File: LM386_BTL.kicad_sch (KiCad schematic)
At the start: 31 parts, among them J1 IN, J2 L_OUT, J3 R_OUT, J4 POWER, U1 LM386, U2 LM386, U3 LM386, U4 LM386

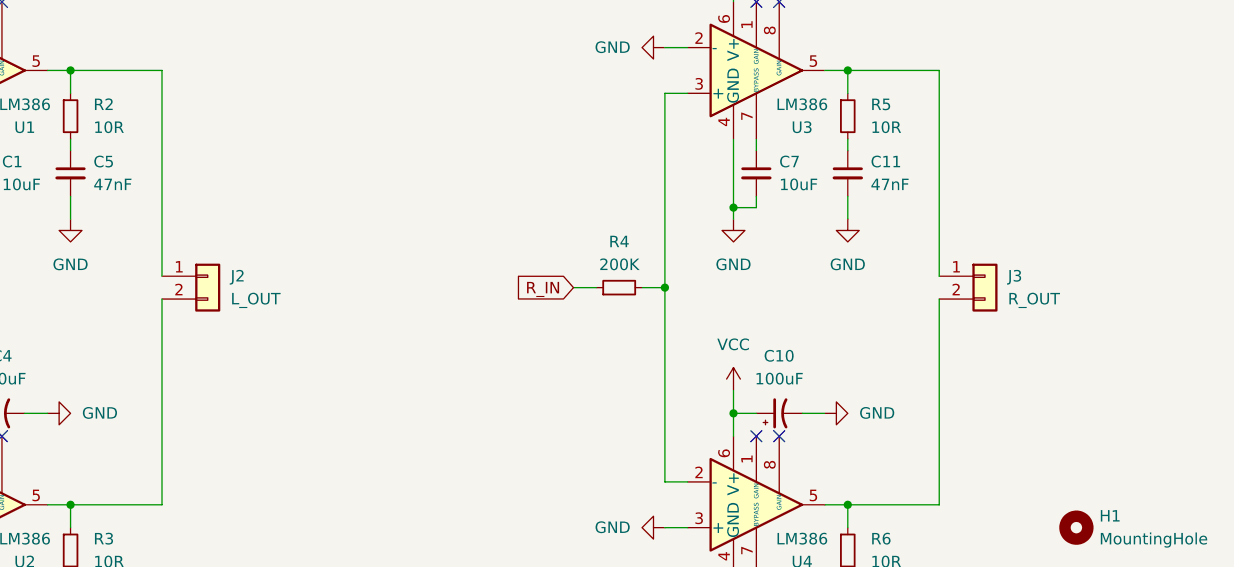
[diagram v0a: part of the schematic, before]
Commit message: Swap positive and negative amplifier position prevent from oscillation
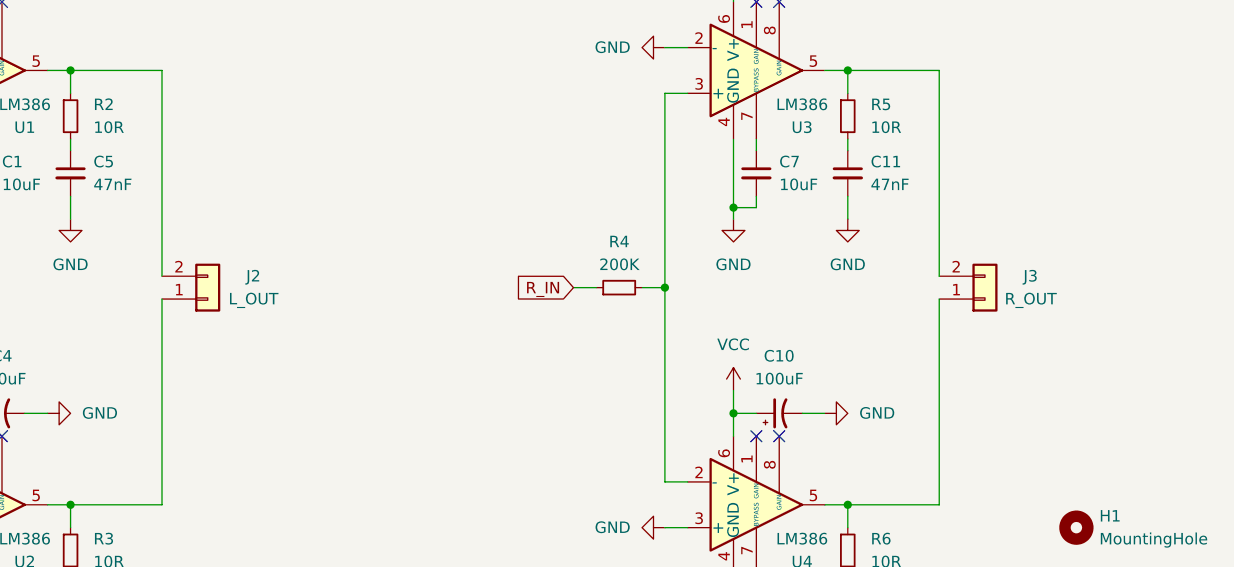
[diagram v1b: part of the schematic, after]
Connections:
- net at R5.1, U3.5: now also J3.2 (Pin_2); no longer J3.1 (Pin_1)
- net at R6.1, U4.5: now also J3.1 (Pin_1); no longer J3.2 (Pin_2)
- net at R2.1, U1.5: now also J2.2 (Pin_2); no longer J2.1 (Pin_1)
- net at R3.1, U2.5: now also J2.1 (Pin_1); no longer J2.2 (Pin_2)
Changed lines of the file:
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@@
   (title_block
     (title "The Ultimate LM386 BTL Amplifier")
-    (date "2022-12-18")
+    (date "2022-12-20")
     (rev "1.0")
     (company "DANCHOUZHOU")
@@
     (pin "1")
   )
-  (symbol (lib_id "Connector_Generic:Conn_01x02") (at 134.62 88.9 0) (unit 1)
-    (in_bom yes) (on_board yes) (fields_autoplaced)
-    (property "Reference" "J2" (id 0) (at 137.16 88.8999 0)
-      (effects (font (size 1.27 1.27)) (justify left))
-    )
-    (property "Value" "L_OUT" (id 1) (at 137.16 91.4399 0)
-      (effects (font (size 1.27 1.27)) (justify left))
-    )
-    (property "Footprint" "Connector_JST:JST_PH_B2B-PH-K_1x02_P2.00mm_Vertical" (id 2) (at 134.62 88.9 0)
-      (effects (font (size 1.27 1.27)) hide)
-    )
-    (property "Datasheet" "~" (id 3) (at 134.62 88.9 0)
+  (symbol (lib_id "Connector_Generic:Conn_01x02") (at 134.62 91.44 0) (mirror x) (unit 1)
+    (in_bom yes) (on_board yes)
+    (property "Reference" "J2" (id 0) (at 139.7 88.9 0))
+    (property "Value" "L_OUT" (id 1) (at 139.7 91.44 0))
+    (property "Footprint" "Connector_JST:JST_PH_B2B-PH-K_1x02_P2.00mm_Vertical" (id 2) (at 134.62 91.44 0)
+      (effects (font (size 1.27 1.27)) hide)
+    )
+    (property "Datasheet" "~" (id 3) (at 134.62 91.44 0)
       (effects (font (size 1.27 1.27)) hide)
     )
@@
     (pin "2")
   )
-  (symbol (lib_id "Connector_Generic:Conn_01x02") (at 220.98 88.9 0) (unit 1)
-    (in_bom yes) (on_board yes) (fields_autoplaced)
-    (property "Reference" "J3" (id 0) (at 223.52 88.8999 0)
-      (effects (font (size 1.27 1.27)) (justify left))
-    )
-    (property "Value" "R_OUT" (id 1) (at 223.52 91.4399 0)
-      (effects (font (size 1.27 1.27)) (justify left))
-    )
-    (property "Footprint" "Connector_JST:JST_PH_B2B-PH-K_1x02_P2.00mm_Vertical" (id 2) (at 220.98 88.9 0)
-      (effects (font (size 1.27 1.27)) hide)
-    )
-    (property "Datasheet" "~" (id 3) (at 220.98 88.9 0)
-      (effects (font (size 1.27 1.27)) hide)
-    )
+  (symbol (lib_id "Connector_Generic:Conn_01x02") (at 220.98 91.44 0) (mirror x) (unit 1)
+    (in_bom yes) (on_board yes)
+    (property "Reference" "J3" (id 0) (at 226.06 88.9 0))
+    (property "Value" "R_OUT" (id 1) (at 226.06 91.44 0))
+    (property "Footprint" "Connector_JST:JST_PH_B2B-PH-K_1x02_P2.00mm_Vertical" (id 2) (at 220.98 91.44 0)
+      (effects (font (size 1.27 1.27)) hide)
+    )
+    (property "Datasheet" "~" (id 3) (at 220.98 91.44 0)
+      (effects (font (size 1.27 1.27)) hide)
+    )

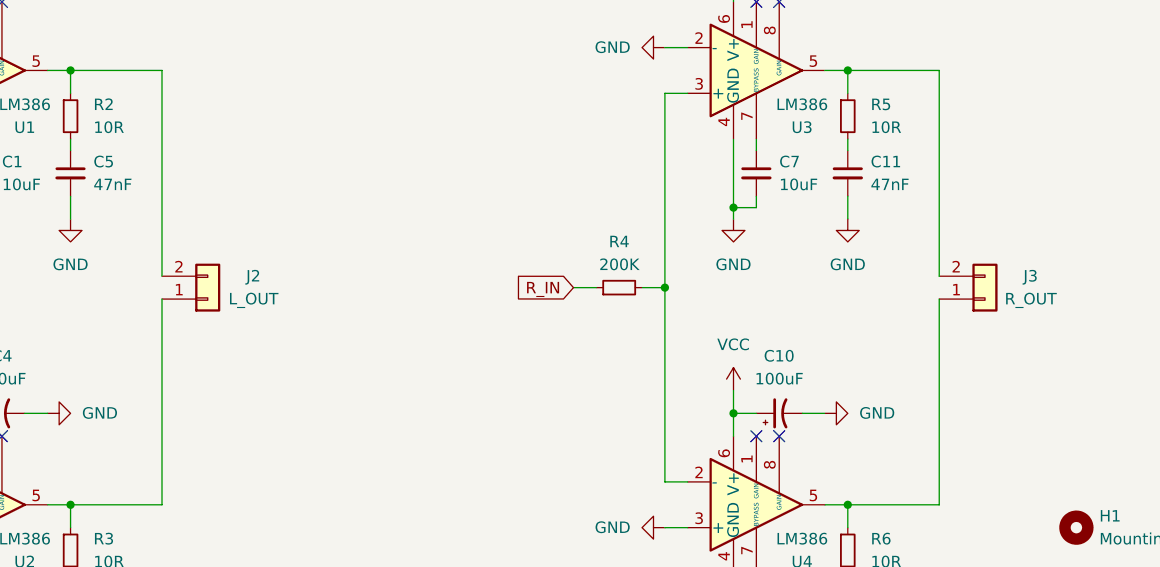
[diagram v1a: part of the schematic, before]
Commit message: Swap output polarity
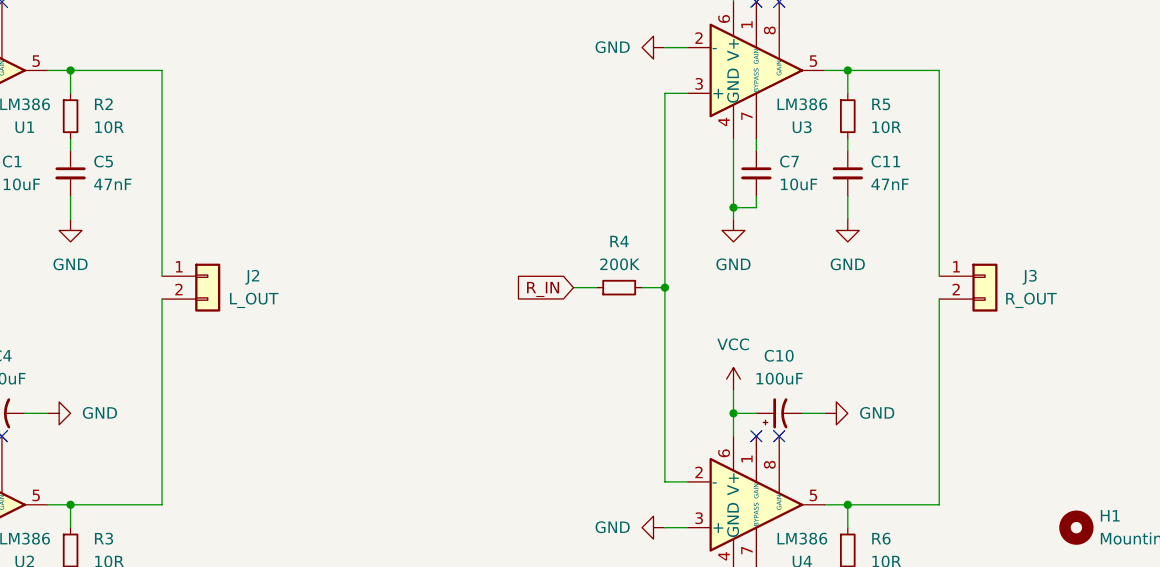
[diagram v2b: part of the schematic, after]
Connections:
- net at R5.1, U3.5: now also J3.1 (Pin_1); no longer J3.2 (Pin_2)
- net at R6.1, U4.5: now also J3.2 (Pin_2); no longer J3.1 (Pin_1)
- net at R3.1, U2.5: now also J2.2 (Pin_2); no longer J2.1 (Pin_1)
- net at R2.1, U1.5: now also J2.1 (Pin_1); no longer J2.2 (Pin_2)
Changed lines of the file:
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@@
     (pin "1")
   )
-  (symbol (lib_id "Connector_Generic:Conn_01x02") (at 134.62 91.44 0) (mirror x) (unit 1)
+  (symbol (lib_id "Connector_Generic:Conn_01x02") (at 134.62 88.9 0) (unit 1)
     (in_bom yes) (on_board yes)
     (property "Reference" "J2" (id 0) (at 139.7 88.9 0))
     (property "Value" "L_OUT" (id 1) (at 139.7 91.44 0))
-    (property "Footprint" "Connector_JST:JST_PH_B2B-PH-K_1x02_P2.00mm_Vertical" (id 2) (at 134.62 91.44 0)
-      (effects (font (size 1.27 1.27)) hide)
-    )
-    (property "Datasheet" "~" (id 3) (at 134.62 91.44 0)
+    (property "Footprint" "Connector_JST:JST_PH_B2B-PH-K_1x02_P2.00mm_Vertical" (id 2) (at 134.62 88.9 0)
+      (effects (font (size 1.27 1.27)) hide)
+    )
+    (property "Datasheet" "~" (id 3) (at 134.62 88.9 0)
       (effects (font (size 1.27 1.27)) hide)
     )
@@
     (pin "2")
   )
-  (symbol (lib_id "Connector_Generic:Conn_01x02") (at 220.98 91.44 0) (mirror x) (unit 1)
+  (symbol (lib_id "Connector_Generic:Conn_01x02") (at 220.98 88.9 0) (unit 1)
     (in_bom yes) (on_board yes)
     (property "Reference" "J3" (id 0) (at 226.06 88.9 0))
     (property "Value" "R_OUT" (id 1) (at 226.06 91.44 0))
-    (property "Footprint" "Connector_JST:JST_PH_B2B-PH-K_1x02_P2.00mm_Vertical" (id 2) (at 220.98 91.44 0)
-      (effects (font (size 1.27 1.27)) hide)
-    )
-    (property "Datasheet" "~" (id 3) (at 220.98 91.44 0)
-      (effects (font (size 1.27 1.27)) hide)
-    )
+    (property "Footprint" "Connector_JST:JST_PH_B2B-PH-K_1x02_P2.00mm_Vertical" (id 2) (at 220.98 88.9 0)
+      (effects (font (size 1.27 1.27)) hide)
+    )
+    (property "Datasheet" "~" (id 3) (at 220.98 88.9 0)
+      (effects (font (size 1.27 1.27)) hide)
+    )

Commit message: Change capacitor footprint P2.50mm into P2.00mm
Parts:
- C1, C10, C2, C3, C4, C7, C8, C9: footprint Capacitor_THT:CP_Radial_D5.0mm_P2.50mm -> Capacitor_THT:CP_Radial_D5.0mm_P2.00mm
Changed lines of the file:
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@@
     (property "Reference" "C10" (id 0) (at 198.12 97.79 90))
     (property "Value" "100uF" (id 1) (at 198.12 100.33 90))
-    (property "Footprint" "Capacitor_THT:CP_Radial_D5.0mm_P2.50mm" (id 2) (at 198.12 104.14 0)
+    (property "Footprint" "Capacitor_THT:CP_Radial_D5.0mm_P2.00mm" (id 2) (at 198.12 104.14 0)
       (effects (font (size 1.27 1.27)) hide)
     )
@@
     (property "Reference" "C9" (id 0) (at 198.12 49.53 90))
     (property "Value" "100uF" (id 1) (at 198.12 52.07 90))
-    (property "Footprint" "Capacitor_THT:CP_Radial_D5.0mm_P2.50mm" (id 2) (at 198.12 55.88 0)
+    (property "Footprint" "Capacitor_THT:CP_Radial_D5.0mm_P2.00mm" (id 2) (at 198.12 55.88 0)
       (effects (font (size 1.27 1.27)) hide)
     )
@@
       (effects (font (size 1.27 1.27)) (justify left))
     )
-    (property "Footprint" "Capacitor_THT:CP_Radial_D5.0mm_P2.50mm" (id 2) (at 195.58 77.47 0)
+    (property "Footprint" "Capacitor_THT:CP_Radial_D5.0mm_P2.00mm" (id 2) (at 195.58 77.47 0)
       (effects (font (size 1.27 1.27)) hide)
     )
@@
     (property "Reference" "C3" (id 0) (at 111.76 49.53 90))
     (property "Value" "100uF" (id 1) (at 111.76 52.07 90))
-    (property "Footprint" "Capacitor_THT:CP_Radial_D5.0mm_P2.50mm" (id 2) (at 111.76 55.88 0)
+    (property "Footprint" "Capacitor_THT:CP_Radial_D5.0mm_P2.00mm" (id 2) (at 111.76 55.88 0)
       (effects (font (size 1.27 1.27)) hide)
     )
@@
     (property "Reference" "C4" (id 0) (at 111.76 97.79 90))
     (property "Value" "100uF" (id 1) (at 111.76 100.33 90))
-    (property "Footprint" "Capacitor_THT:CP_Radial_D5.0mm_P2.50mm" (id 2) (at 111.76 104.14 0)
+    (property "Footprint" "Capacitor_THT:CP_Radial_D5.0mm_P2.00mm" (id 2) (at 111.76 104.14 0)
       (effects (font (size 1.27 1.27)) hide)
     )
@@
       (effects (font (size 1.27 1.27)) (justify left))
     )
-    (property "Footprint" "Capacitor_THT:CP_Radial_D5.0mm_P2.50mm" (id 2) (at 109.22 125.73 0)
+    (property "Footprint" "Capacitor_THT:CP_Radial_D5.0mm_P2.00mm" (id 2) (at 109.22 125.73 0)
       (effects (font (size 1.27 1.27)) hide)
     )
@@
       (effects (font (size 1.27 1.27)) (justify left))
     )
-    (property "Footprint" "Capacitor_THT:CP_Radial_D5.0mm_P2.50mm" (id 2) (at 195.58 125.73 0)
+    (property "Footprint" "Capacitor_THT:CP_Radial_D5.0mm_P2.00mm" (id 2) (at 195.58 125.73 0)
       (effects (font (size 1.27 1.27)) hide)
     )
@@
       (effects (font (size 1.27 1.27)) (justify left))
     )
-    (property "Footprint" "Capacitor_THT:CP_Radial_D5.0mm_P2.50mm" (id 2) (at 109.22 77.47 0)
+    (property "Footprint" "Capacitor_THT:CP_Radial_D5.0mm_P2.00mm" (id 2) (at 109.22 77.47 0)
       (effects (font (size 1.27 1.27)) hide)
     )
@@
     )
     (path "/e0d5a886-0139-4980-a4d1-889d25bae079"
-      (reference "C1") (unit 1) (value "10uF") (footprint "Capacitor_THT:CP_Radial_D5.0mm_P2.50mm")
+      (reference "C1") (unit 1) (value "10uF") (footprint "Capacitor_THT:CP_Radial_D5.0mm_P2.00mm")
     )
     (path "/a442bb95-f32f-4e77-af00-12dc6f8caf89"
-      (reference "C2") (unit 1) (value "10uF") (footprint "Capacitor_THT:CP_Radial_D5.0mm_P2.50mm")
+      (reference "C2") (unit 1) (value "10uF") (footprint "Capacitor_THT:CP_Radial_D5.0mm_P2.00mm")
     )
     (path "/366ee859-b2d1-493c-a89b-f6a316859c66"
-      (reference "C3") (unit 1) (value "100uF") (footprint "Capacitor_THT:CP_Radial_D5.0mm_P2.50mm")
+      (reference "C3") (unit 1) (value "100uF") (footprint "Capacitor_THT:CP_Radial_D5.0mm_P2.00mm")
     )
     (path "/3d3efd5e-d1b0-4e1b-970c-55c7a3153876"
-      (reference "C4") (unit 1) (value "100uF") (footprint "Capacitor_THT:CP_Radial_D5.0mm_P2.50mm")
+      (reference "C4") (unit 1) (value "100uF") (footprint "Capacitor_THT:CP_Radial_D5.0mm_P2.00mm")
     )
     (path "/a0e4126d-6699-41aa-985b-3b1953236e66"
@@
     )
     (path "/2e9436f9-d546-4341-aea8-415e1ba22fc1"
-      (reference "C7") (unit 1) (value "10uF") (footprint "Capacitor_THT:CP_Radial_D5.0mm_P2.50mm")
+      (reference "C7") (unit 1) (value "10uF") (footprint "Capacitor_THT:CP_Radial_D5.0mm_P2.00mm")
     )
     (path "/b2b9e2b0-f6bc-4280-87f5-ecb71306e932"
-      (reference "C8") (unit 1) (value "10uF") (footprint "Capacitor_THT:CP_Radial_D5.0mm_P2.50mm")
+      (reference "C8") (unit 1) (value "10uF") (footprint "Capacitor_THT:CP_Radial_D5.0mm_P2.00mm")
     )
     (path "/12d48a2d-fcb4-4942-8d7b-8ddf5a94125f"
-      (reference "C9") (unit 1) (value "100uF") (footprint "Capacitor_THT:CP_Radial_D5.0mm_P2.50mm")
+      (reference "C9") (unit 1) (value "100uF") (footprint "Capacitor_THT:CP_Radial_D5.0mm_P2.00mm")
     )
     (path "/0c2d1b3e-056e-4a75-bfd2-33ced4733e93"
-      (reference "C10") (unit 1) (value "100uF") (footprint "Capacitor_THT:CP_Radial_D5.0mm_P2.50mm")
+      (reference "C10") (unit 1) (value "100uF") (footprint "Capacitor_THT:CP_Radial_D5.0mm_P2.00mm")
     )
     (path "/9b076e9d-5343-47f6-8198-7c952f787632"
